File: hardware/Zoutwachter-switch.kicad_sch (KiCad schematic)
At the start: 17 parts, among them J1 Output connector, J2 SWD Pin Header, J3 SWD-TagConnect, J4 I2C control port, J5 Zoutwachter cable, SW1 RESET, U1 STM32L071CBTx, Y1 8MHz

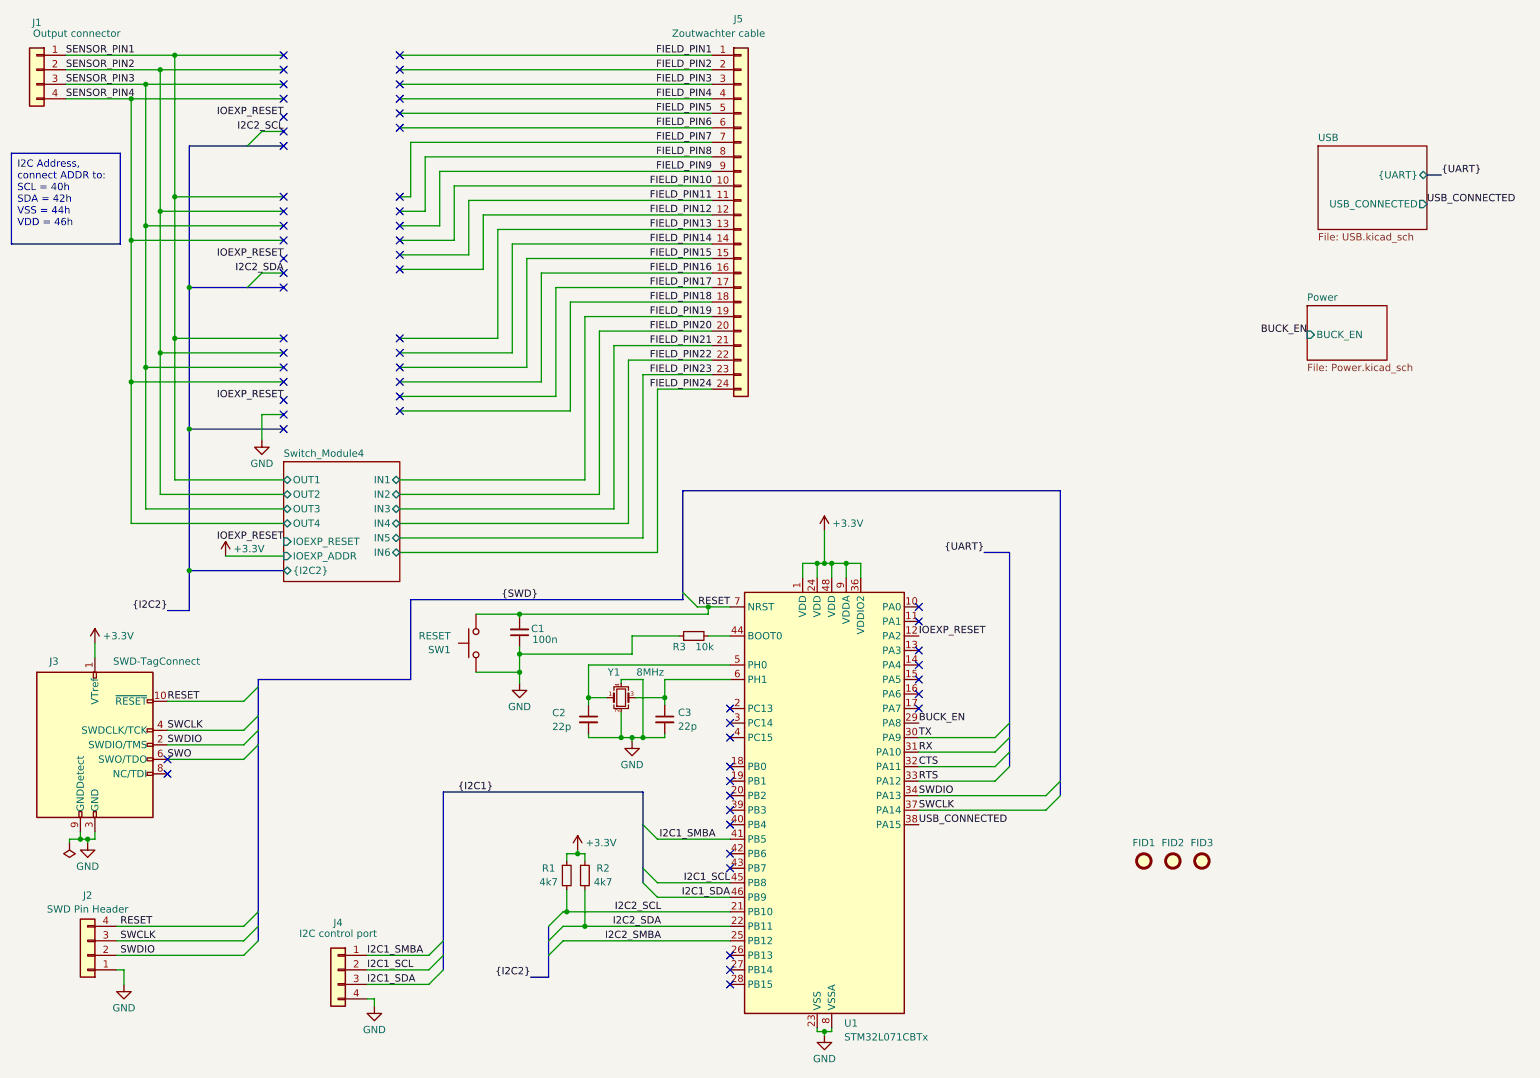
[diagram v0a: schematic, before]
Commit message: feat(RGB): WS2812B driver
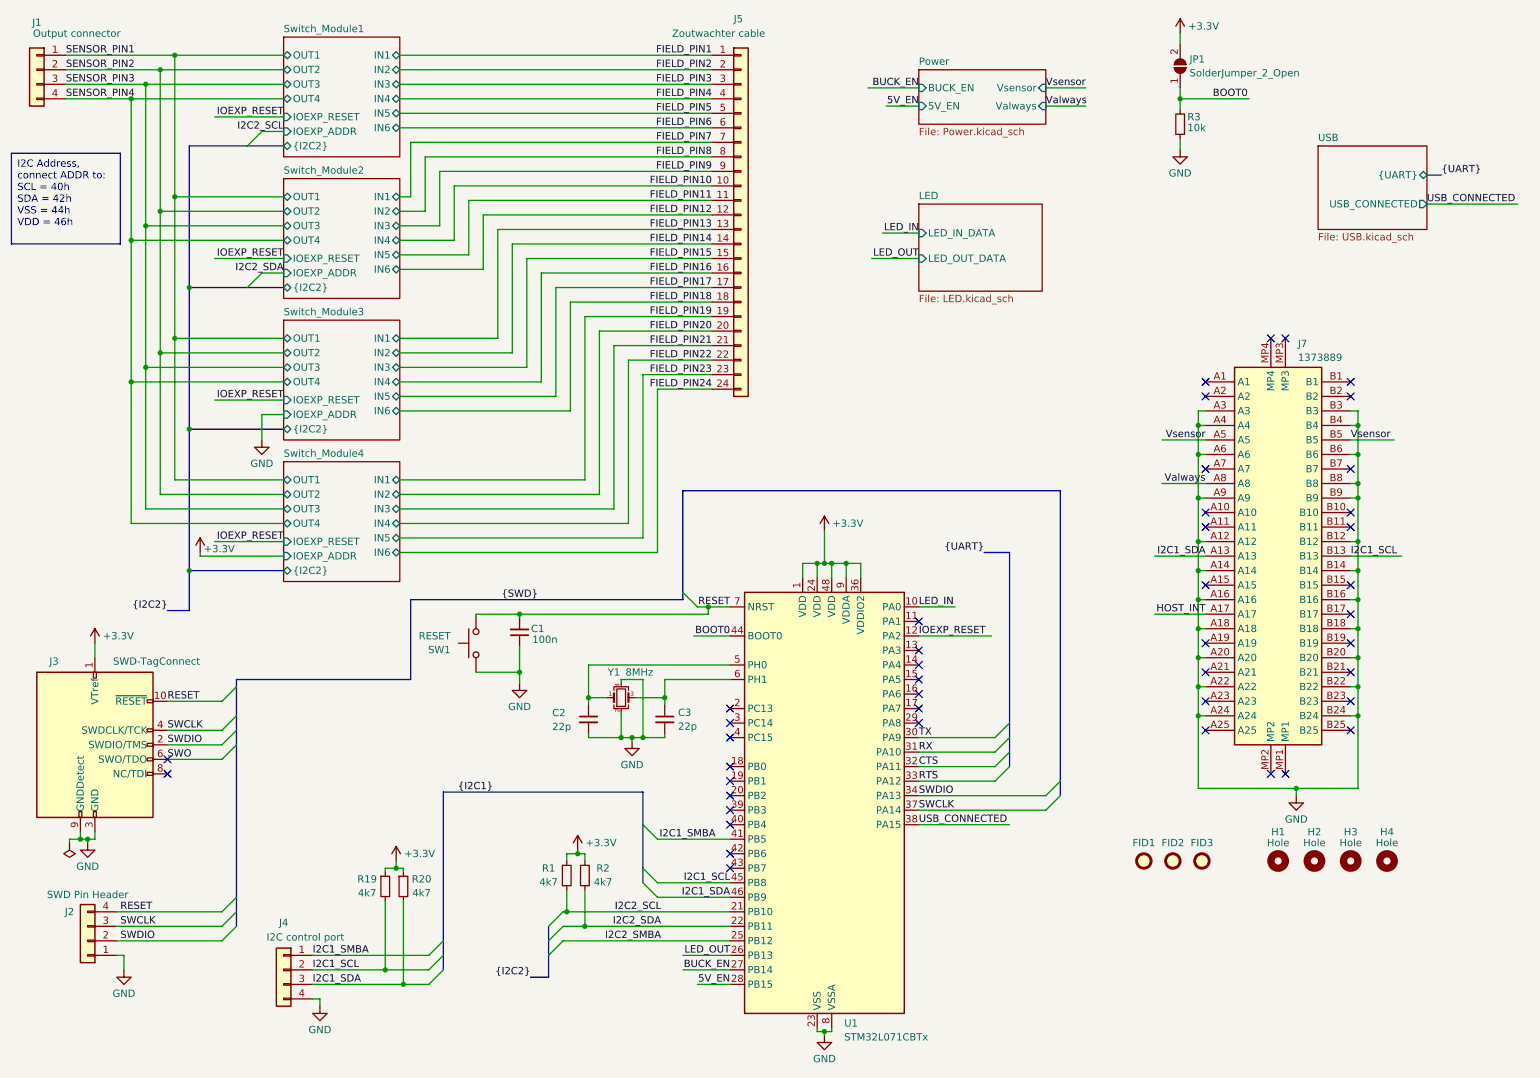
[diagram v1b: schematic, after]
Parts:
- added H1, H2, H3, H4: Hole, MountingHole:MountingHole_3.2mm_M3, symbol Mechanical:MountingHole
- added J7: 1373889, Phoenix Contact 1373889:1373889, symbol Phoenix Contact 1373889:1373889
- added JP1: SolderJumper_2_Open, Jumper:SolderJumper-2_P1.3mm_Open_RoundedPad1.0x1.5mm, symbol Jumper:SolderJumper_2_Open
- added R19, R20: 4k7, Resistor_SMD:R_0603_1608Metric, symbol Device:R_Small
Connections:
- net +3V3: now also JP1.2 (B), R19.1, R20.1
- net BUCK_EN: now also U1.27 (PB14); no longer U1.29 (PA8)
- net GND: now also J7.A12, J7.A14, J7.A16, J7.A18, J7.A20, J7.A22, J7.A24, J7.A3, J7.A4, J7.A6, J7.A9, J7.B12, J7.B14, J7.B16, J7.B18, J7.B20, J7.B22, J7.B24, J7.B3, J7.B4, J7.B6, J7.B8, J7.B9
- net I2C1_SCL: now also J7.B13, R19.2
- net I2C1_SDA: now also J7.A13, R20.2
- net BOOT0: now reaches R3.2, U1.44 (BOOT0)
- net BOOT0: now also JP1.1 (A)
- net LED_IN: now reaches U1.10 (PA0)
- net LED_OUT: now reaches U1.26 (PB13)
- net 5V_EN: now reaches U1.28 (PB15)
- new net HOST_INT: J7.A17
- new net Valways: J7.A8
- new net Vsensor: J7.A5, J7.B5
- no-connect marks 61 -> 44
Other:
- added sheet LED (LED.kicad_sch)
- added sheet Switch_Module1 (Switch.kicad_sch)
- added sheet Switch_Module2 (Switch.kicad_sch)
- added sheet Switch_Module3 (Switch.kicad_sch)
- sheet Power ports: added 5V_EN, Valways, Vsensor; removed none
- moved on the sheet: J2, J4, R3
